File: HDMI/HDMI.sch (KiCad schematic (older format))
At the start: 43 parts, among them J2 PMOD, P1 HDMI-D, U1 NCP1402SN33T1G, U2 PCA9306

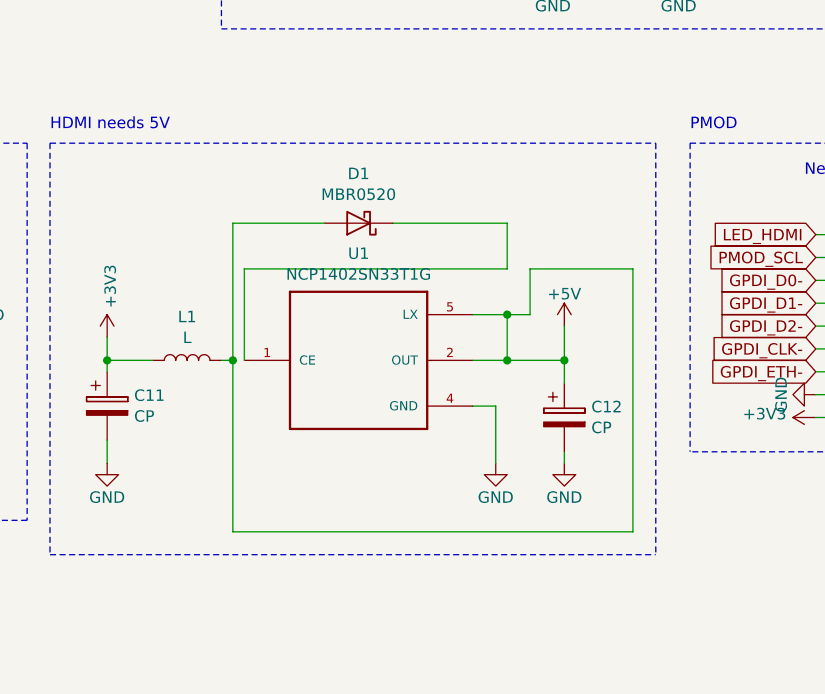
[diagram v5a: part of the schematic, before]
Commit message: Changing DC-DC - rerouting
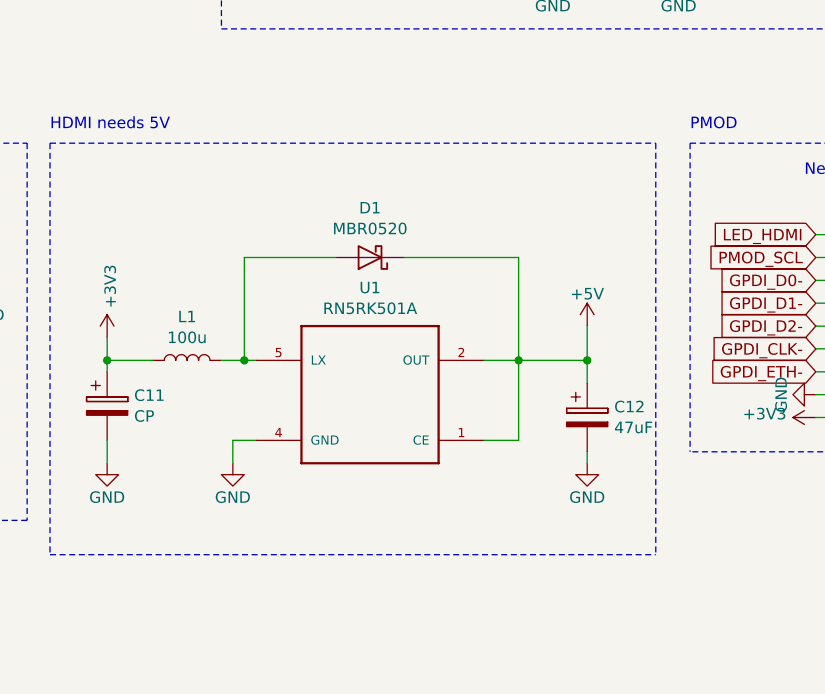
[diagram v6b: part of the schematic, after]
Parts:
- removed U1: NCP1402SN33T1G, NCP1402SN33T1G:SOT95P275X110-5N, symbol HDMI-rescue:NCP1402SN33T1G-NCP1402SN33T1G
- added U1: RN5RK501A, Package_TO_SOT_SMD:SOT-23-5_HandSoldering, symbol HDMI-rescue:RN5RK501A
- C12: value CP -> 47uF
- L1: value L -> 100u
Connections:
- net +5V: now also D1.1 (K), U1.1 (CE), U1.2 (OUT); no longer D1.2 (A), L1.2
- net GND: now also U1.4 (GND)
- new net: D1.2 (A), L1.2, U1.5 (LX)
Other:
- moved on the sheet: C12, D1
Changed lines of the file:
@@
 PCB v1.8.1 and higher accept FCI 10029449-111RLF\nwww.amphenol-icc.com\nmouser PN: 649-10029449-111RLF\nhttp://portal.fciconnect.com/Comergent/fci/drawing/10029449.pdf\n\nPCB v1.7 and v1.8 accept\nmouser PN: 538-47151-1001 (Molex)\nhttps://www.molex.com/pdm_docs/sd/471511001_sd.pdf\nmouser PN: 710-685119134923 (Wurth)\nhttps://katalog.we-online.com/em/datasheet/685119134923.pdf
-$Comp
-L HDMI-rescue:NCP1402SN33T1G-NCP1402SN33T1G U1
-U 1 1 5C00523C
-P 6550 4500
-F 0 "U1" H 6550 4967 50  0000 C CNN
-F 1 "NCP1402SN33T1G" H 6550 4876 50  0000 C CNN
-F 2 "NCP1402SN33T1G:SOT95P275X110-5N" H 6550 4500 50  0001 L BNN
-F 3 "NCP1402 Series 6 V 200 mA PFM Step-Up Micropower Switching Regulator - SOT-23-5" H 6550 4500 50  0001 L BNN
-F 4 "Unavailable" H 6550 4500 50  0001 L BNN "Field4"
-F 5 "ON Semiconductor" H 6550 4500 50  0001 L BNN "Field5"
-F 6 "SOT-23 ON Semiconductor" H 6550 4500 50  0001 L BNN "Field6"
-F 7 "None" H 6550 4500 50  0001 L BNN "Field7"
-F 8 "NCP1402SN33T1G" H 6550 4500 50  0001 L BNN "Field8"
-	1    6550 4500
-	1    0    0    -1
-$EndComp
 $Comp
 L Device:CP C12
 U 1 1 5C0053C4
-P 7450 4750
-F 0 "C12" H 7568 4796 50  0000 L CNN
-F 1 "CP" H 7568 4705 50  0000 L CNN
-F 2 "Capacitor_Tantalum_SMD:CP_EIA-3216-10_Kemet-I" H 7488 4600 50  0001 C CNN
-F 3 "~" H 7450 4750 50  0001 C CNN
-	1    7450 4750
+P 7550 4750
+F 0 "C12" H 7668 4796 50  0000 L CNN
+F 1 "47uF" H 7668 4705 50  0000 L CNN
+F 2 "Capacitor_Tantalum_SMD:CP_EIA-3216-10_Kemet-I" H 7588 4600 50  0001 C CNN
+F 3 "~" H 7550 4750 50  0001 C CNN
+	1    7550 4750
 	1    0    0    -1
 $EndComp
@@
 P 5800 4500
 F 0 "L1" V 5990 4500 50  0000 C CNN
-F 1 "L" V 5899 4500 50  0000 C CNN
+F 1 "100u" V 5899 4500 50  0000 C CNN
 F 2 "Inductor_SMD:L_1210_3225Metric_Pad1.42x2.65mm_HandSolder" H 5800 4500 50  0001 C CNN
 F 3 "~" H 5800 4500 50  0001 C CNN
@@
 L Diode:MBR0520 D1
 U 1 1 5C00579C
-P 6550 3900
-F 0 "D1" H 6550 3684 50  0000 C CNN
-F 1 "MBR0520" H 6550 3775 50  0000 C CNN
-F 2 "Diode_SMD:D_SOD-123" H 6550 3725 50  0001 C CNN
-F 3 "http://www.mccsemi.com/up_pdf/MBR0520~MBR0580(SOD123).pdf" H 6550 3900 50  0001 C CNN
-	1    6550 3900
+P 6600 4050
+F 0 "D1" H 6600 3834 50  0000 C CNN
+F 1 "MBR0520" H 6600 3925 50  0000 C CNN
+F 2 "Diode_SMD:D_SOD-123" H 6600 3875 50  0001 C CNN
+F 3 "http://www.mccsemi.com/up_pdf/MBR0520~MBR0580(SOD123).pdf" H 6600 4050 50  0001 C CNN
+	1    6600 4050
 	-1   0    0    1
 $EndComp
@@
 L power:+5V #PWR0105
 U 1 1 5C007648
-P 7450 4350
-F 0 "#PWR0105" H 7450 4200 50  0001 C CNN
-F 1 "+5V" H 7450 4490 50  0000 C CNN
-F 2 "" H 7450 4350 50  0000 C CNN
-F 3 "" H 7450 4350 50  0000 C CNN
-	1    7450 4350
+P 7550 4350
+F 0 "#PWR0105" H 7550 4200 50  0001 C CNN
+F 1 "+5V" H 7550 4490 50  0000 C CNN
+F 2 "" H 7550 4350 50  0000 C CNN
+F 3 "" H 7550 4350 50  0000 C CNN
+	1    7550 4350
 	-1   0    0    -1
 $EndComp
@@
 L power:GND #PWR0106
 U 1 1 5C007675
-P 7450 4950
-F 0 "#PWR0106" H 7450 4700 50  0001 C CNN
-F 1 "GND" H 7450 4800 50  0000 C CNN
-F 2 "" H 7450 4950 60  0000 C CNN
-F 3 "" H 7450 4950 60  0000 C CNN
-	1    7450 4950
+P 7550 4950
+F 0 "#PWR0106" H 7550 4700 50  0001 C CNN
+F 1 "GND" H 7550 4800 50  0000 C CNN
+F 2 "" H 7550 4950 60  0000 C CNN
+F 3 "" H 7550 4950 60  0000 C CNN
+	1    7550 4950
 	-1   0    0    -1
 $EndComp
@@
 	1    5450 4400
 	1    0    0    -1
-$EndComp
-$Comp
-L power:GND #PWR0108
-U 1 1 5C009295
-P 7150 4950
-F 0 "#PWR0108" H 7150 4700 50  0001 C CNN
-F 1 "GND" H 7150 4800 50  0000 C CNN
-F 2 "" H 7150 4950 60  0000 C CNN
-F 3 "" H 7150 4950 60  0000 C CNN
-	1    7150 4950
-	-1   0    0    -1
 $EndComp
 $Comp
@@
 $EndComp
 Wire Wire Line
-	7150 4950 7150 4700
-Wire Wire Line
-	7150 4700 7050 4700
-Wire Wire Line
-	7050 4500 7200 4500
-Wire Wire Line
-	7450 4500 7450 4600
-Wire Wire Line
-	7450 4950 7450 4900
-Wire Wire Line
-	7450 4350 7450 4500
-Connection ~ 7450 4500
-Wire Wire Line
-	7200 4500 7200 4300
-Wire Wire Line
-	7200 4300 7050 4300
-Connection ~ 7200 4500
-Wire Wire Line
-	7200 4500 7450 4500
+	7550 4950 7550 4900
 Wire Wire Line
 	5650 4500 5450 4500
@@
 Wire Wire Line
 	5450 4400 5450 4500
-Wire Wire Line
-	5950 4500 6000 4500
-Wire Wire Line
-	6700 3900 7200 3900
-Wire Wire Line
-	6400 3900 6000 3900
-Wire Wire Line
-	6000 3900 6000 4500
 Wire Wire Line
 	5450 4850 5450 4950
@@
 	1950 2750 3750 2750
 Wire Wire Line
-	7200 3900 7200 4100
-Wire Wire Line
-	7200 4100 6050 4100
-Wire Wire Line
-	6050 4100 6050 4500
-Wire Wire Line
-	6000 4500 6000 5250
-Wire Wire Line
-	6000 5250 7750 5250
-Wire Wire Line
-	7750 5250 7750 4100
-Wire Wire Line
-	7750 4100 7300 4100
-Wire Wire Line
-	7300 4100 7300 4300
-Wire Wire Line
-	7300 4300 7200 4300
-Connection ~ 6000 4500
-Connection ~ 7200 4300
+	7550 4350 7550 4500
+$Comp
+L HDMI-rescue:RN5RK501A U1
+U 1 1 5E4C8F89
+P 6600 4650
+F 0 "U1" H 6600 5117 50  0000 C CNN
+F 1 "RN5RK501A" H 6600 5026 50  0000 C CNN
+F 2 "Package_TO_SOT_SMD:SOT-23-5_HandSoldering" H 6600 5150 50  0001 L BNN
+F 3 "Switching Voltage Regulators 8V Input VFM Step-up DCDC Converter " H 6450 5050 50  0001 L BNN
+F 4 "Ricoh Electronic Devices Company " H 6750 5350 50  0001 L BNN "Field5"
+F 5 "SOT-23 ON Semiconductor" H 6650 5250 50  0001 L BNN "Field6"
+F 6 "None" H 6900 5550 50  0001 L BNN "Field7"
+F 7 "RN5RK501A" H 6850 5450 50  0001 L BNN "Field8"
+	1    6600 4650
+	1    0    0    -1
+$EndComp
+Wire Wire Line
+	5950 4500 6050 4500
+Wire Wire Line
+	6050 4500 6050 4050
+Wire Wire Line
+	6050 4050 6450 4050
+Connection ~ 6050 4500
+Wire Wire Line
+	6050 4500 6100 4500
+Wire Wire Line
+	6750 4050 7250 4050
+Wire Wire Line
+	7250 4050 7250 4500
+Wire Wire Line
+	7250 4500 7100 4500
+Wire Wire Line
+	7250 4500 7250 4850
+Wire Wire Line
+	7250 4850 7100 4850
+Connection ~ 7250 4500
+$Comp
+L power:GND #PWR0108
+U 1 1 5E4DFBDE
+P 6000 4950
+F 0 "#PWR0108" H 6000 4700 50  0001 C CNN
+F 1 "GND" H 6000 4800 50  0000 C CNN
+F 2 "" H 6000 4950 60  0000 C CNN
+F 3 "" H 6000 4950 60  0000 C CNN
+	1    6000 4950
+	-1   0    0    -1
+$EndComp
+Wire Wire Line
+	6000 4950 6000 4850
+Wire Wire Line
+	6000 4850 6100 4850
+Wire Wire Line
+	7250 4500 7550 4500
+Connection ~ 7550 4500
+Wire Wire Line
+	7550 4500 7550 4600
 $EndSCHEMATC

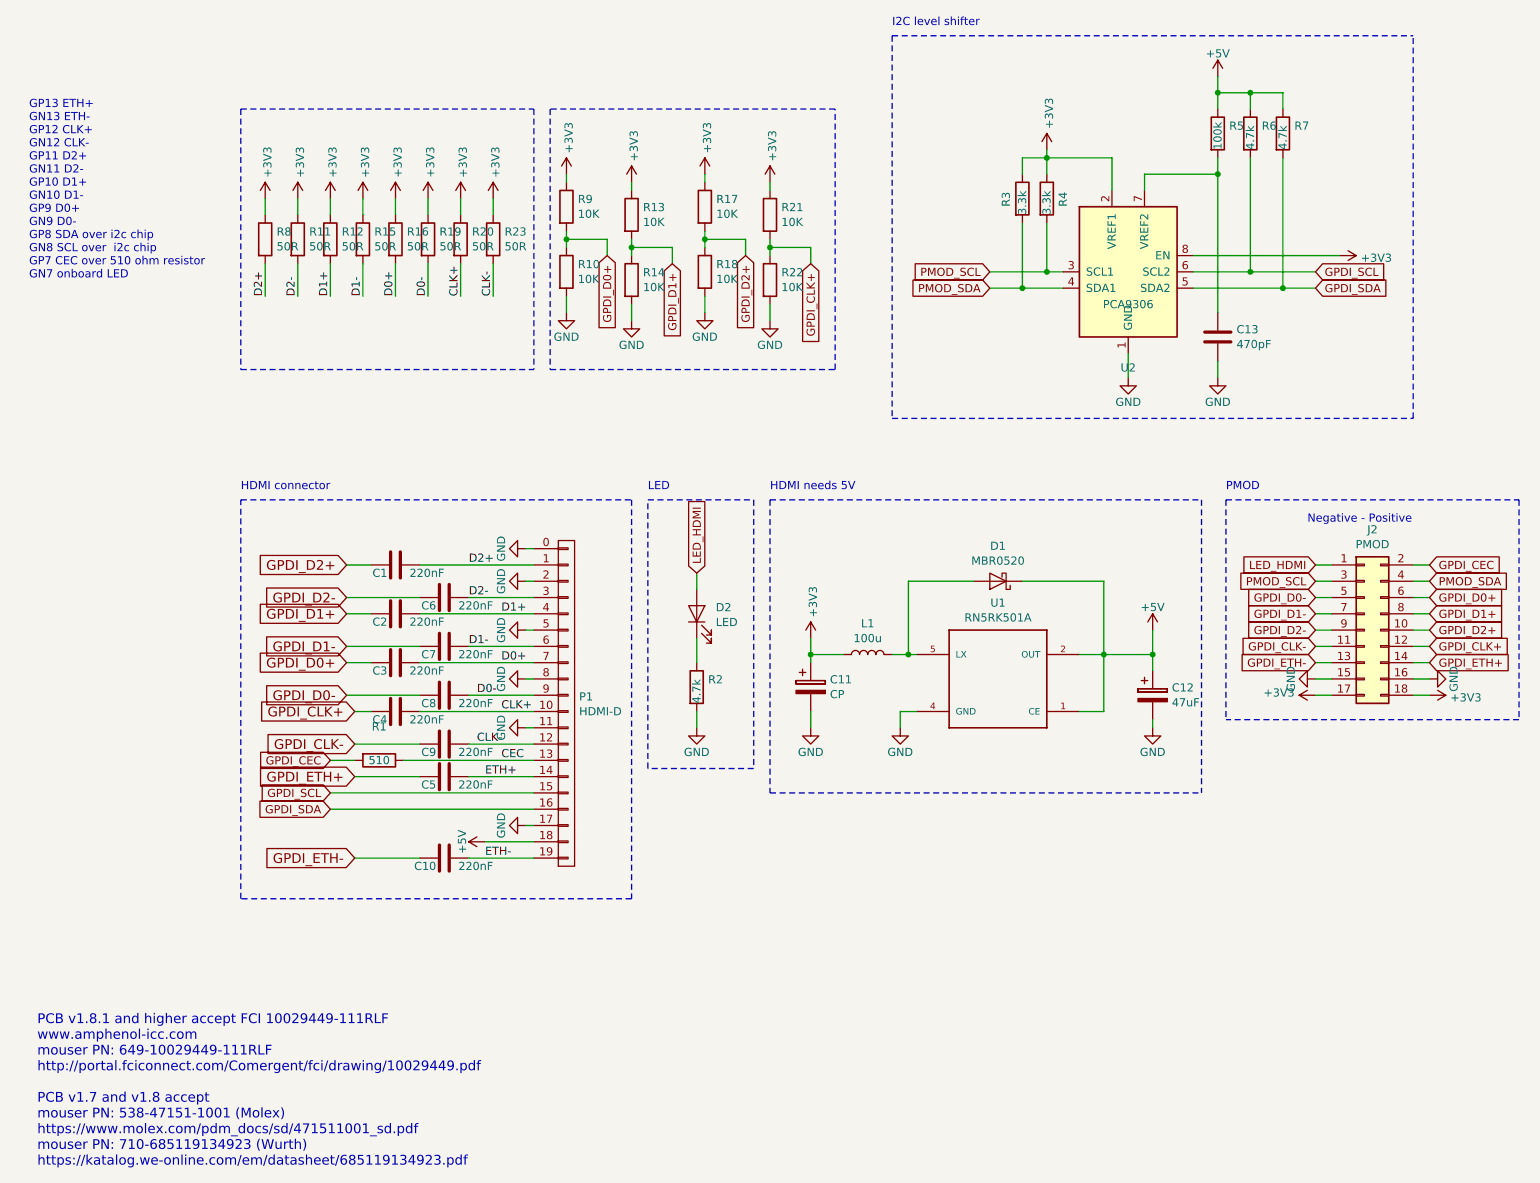
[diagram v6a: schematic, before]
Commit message: Adding jumpers and diff termination to shematics
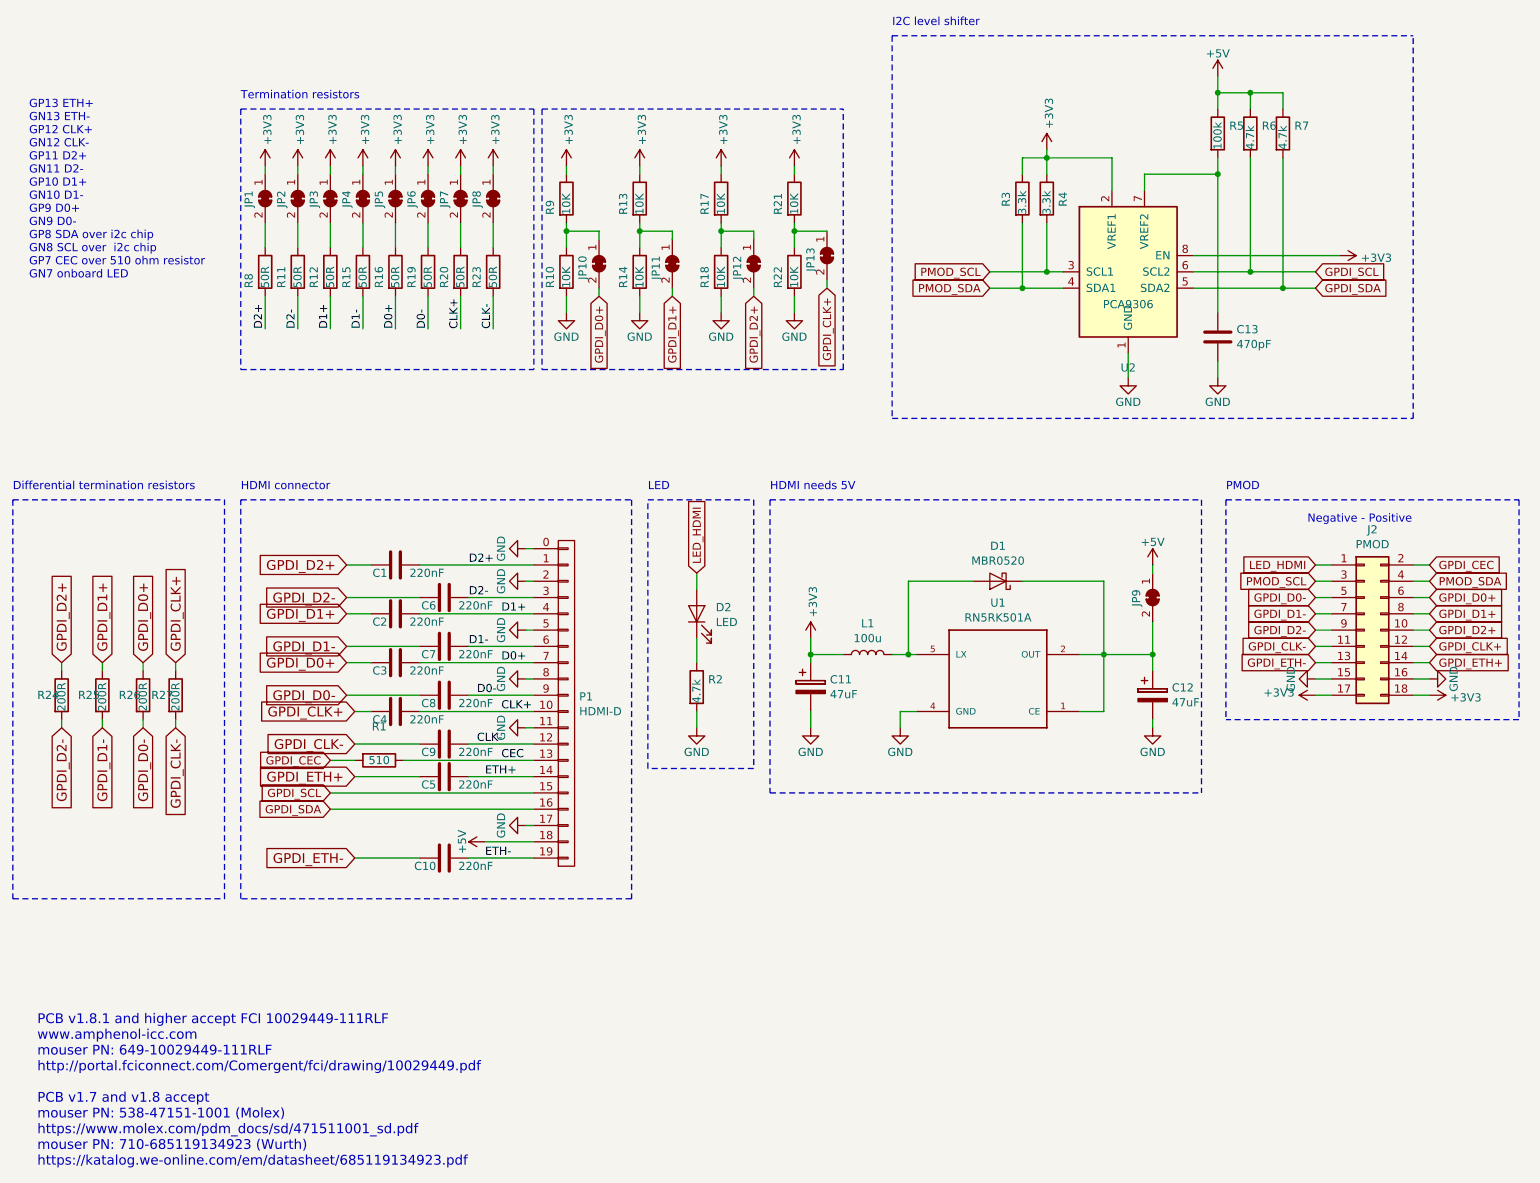
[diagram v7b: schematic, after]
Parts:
- added JP1, JP10, JP11, JP12, JP13, JP2, JP3, JP4, JP5, JP6, JP7, JP8, JP9: JUMP, Jumper:SolderJumper-2_P1.3mm_Bridged_RoundedPad1.0x1.5mm, symbol Jumper:SolderJumper_2_Bridged
- added R24, R25, R26, R27: 200R, Resistor_SMD:R_0603_1608Metric_Pad1.05x0.95mm_HandSolder, symbol antena:R
- C11: value CP -> 47uF
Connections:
- net +3V3: now also JP1.1 (A), JP2.1 (A), JP3.1 (A), JP4.1 (A), JP5.1 (A), JP6.1 (A), JP7.1 (A), JP8.1 (A); no longer R11.1, R12.1, R15.1, R16.1, R19.1, R20.1, R23.1, R8.1
- net +5V: now also JP9.1 (A); no longer C12.1, D1.1 (K), U1.1 (CE), U1.2 (OUT)
- net GPDI_CLK+: now also JP13.2 (B), R27.1; no longer R21.2, R22.1
- net GPDI_CLK-: now also R27.2
- net GPDI_D0+: now also JP10.2 (B), R26.1; no longer R10.1, R9.2
- net GPDI_D0-: now also R26.2
- net GPDI_D1+: now also JP11.2 (B), R25.1; no longer R13.2, R14.1
- net GPDI_D1-: now also R25.2
- net GPDI_D2+: now also JP12.2 (B), R24.1; no longer R17.2, R18.1
- net GPDI_D2-: now also R24.2
- new net: C12.1, D1.1 (K), JP9.2 (B), U1.1 (CE), U1.2 (OUT)
- new net: JP2.2 (B), R11.1
- new net: JP3.2 (B), R12.1
- new net: JP4.2 (B), R15.1
- new net: JP5.2 (B), R16.1
- new net: JP6.2 (B), R19.1
- new net: JP7.2 (B), R20.1
- new net: JP1.2 (B), R8.1
- new net: JP8.2 (B), R23.1
- new net: JP13.1 (A), R21.2, R22.1
- new net: JP12.1 (A), R17.2, R18.1
- new net: JP11.1 (A), R13.2, R14.1
- new net: JP10.1 (A), R10.1, R9.2
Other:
- note added: "Differential termination resistors"
- note added: "Termination resistors"
- moved on the sheet: R11, R12, R13, R14, R15, R16, R17, R18, R19, R20, R21, R22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
